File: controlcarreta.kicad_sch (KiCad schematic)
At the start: 38 parts, among them J1 Screw_Terminal_01x02, J1255 Conn_Coaxial, J18 FTDI_AUTOPROG, J2 Screw_Terminal_01x02, J3 Conn_01x04_Male, Q1 SI4447ADY-T1-GE3, Q2 SS8050, Q3 SS8050, SW1 RESET, SW2 BOOT, U1 ESP32-S3-WROOM-1-N8

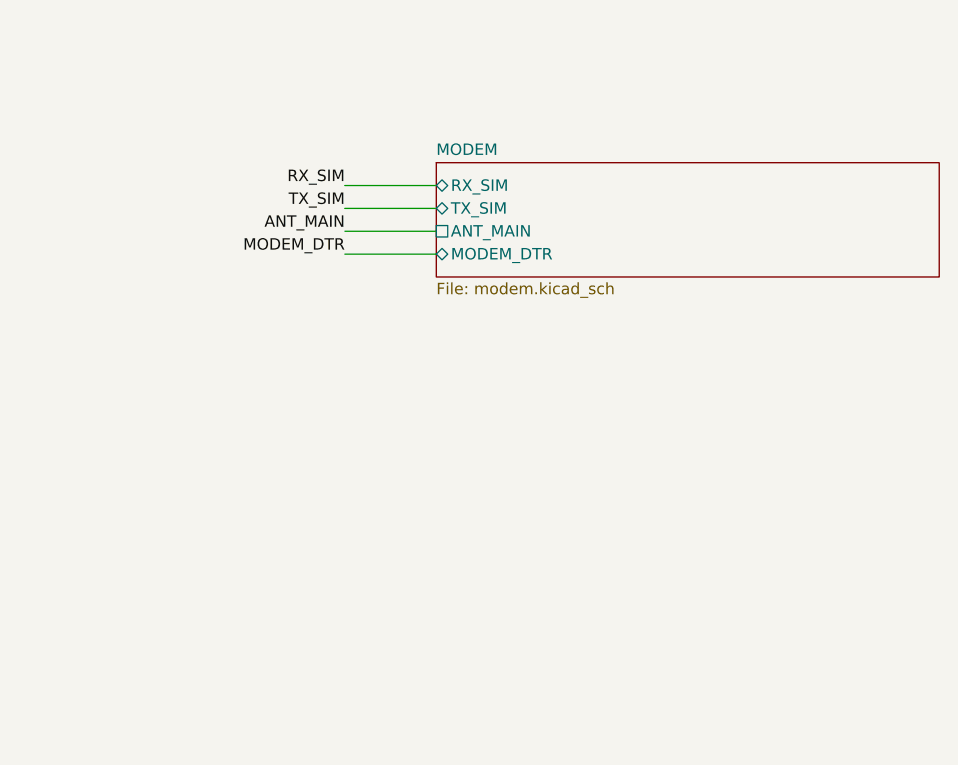
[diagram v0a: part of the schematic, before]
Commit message: modem: 2a via de antena ANT_GNSS (J19 u.FL + J20 SMA) para GPS
El EG25-G / SIM7600 llevan receptor GNSS integrado pero necesitan
antena propia; el esquematico solo tenia ANT_MAIN. Se anade una 2a via
RF identica en topologia a ANT_MAIN:
 - modem.kicad_sch: J19 (u.FL Hirose) -> hierarchical_label ANT_GNSS,
   blindaje a GND (#PWR0563). Pigtail u.FL-u.FL a la toma GNSS de la
   tarjeta Mini-PCIe.
 - controlcarreta.kicad_sch: pin de hoja ANT_GNSS + J20 (SMA Amphenol)
   en la net ANT_GNSS, blindaje a GND (#PWR0564). Caja de la hoja MODEM
   ampliada (12.7 -> 17.78 mm) para alojar los 2 pines nuevos.
 - Poblar J19 O J20 (no ambos). Antena GNSS pasiva, vista al cielo,
   >=3 cm de ANT_MAIN.

ERC sin cambios (370 warnings, 0 errores).

Co-Authored-By: Claude Sonnet 5 <noreply@anthropic.com>
Claude-Session: https://claude.ai/code/session_01T7LXaJdHR17hwkEUJr3uCL
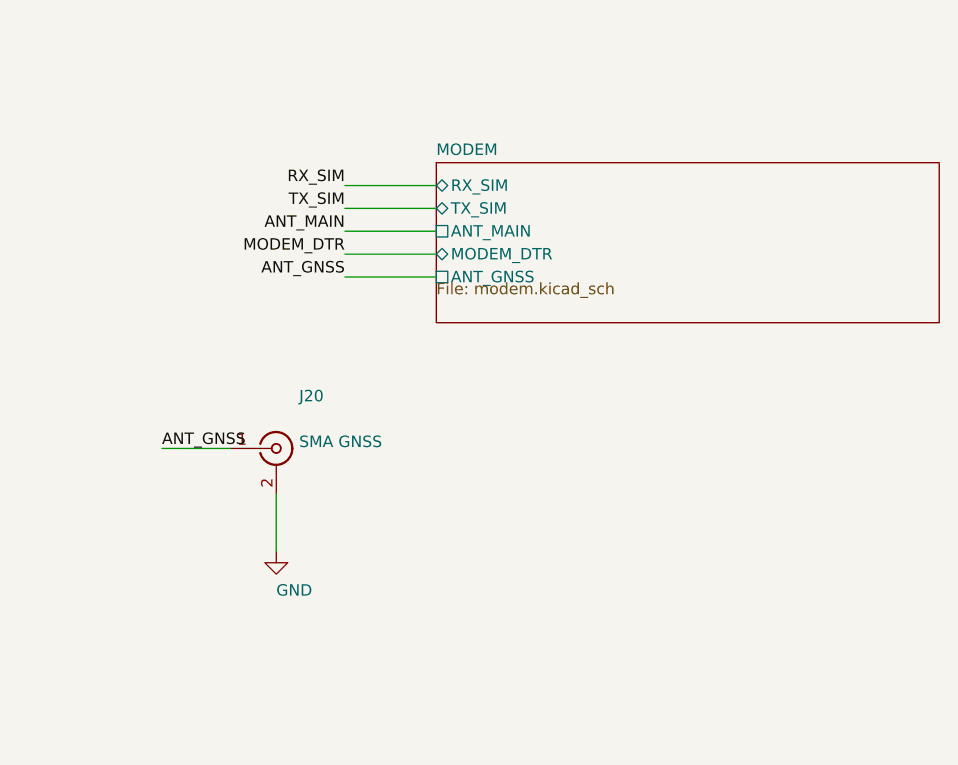
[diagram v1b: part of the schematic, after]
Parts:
- added J20: SMA GNSS, Connector_Coaxial:SMA_Amphenol_132134-16_Vertical, symbol Connector:Conn_Coaxial
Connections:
- net GND: now also J20.2 (Ext)
- new net ANT_GNSS: J20.1 (In)
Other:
- sheet MODEM ports: added ANT_GNSS; removed none
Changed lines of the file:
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@@
 	(wire
 		(pts
+			(xy 330.2 109.22) (xy 320.04 109.22)
+		)
+		(stroke
+			(width 0)
+			(type default)
+		)
+	)
+	(label "ANT_GNSS"
+		(at 320.04 109.22 0)
+		(effects
+			(font
+				(size 1.27 1.27)
+			)
+			(justify right bottom)
+		)
+	)
+	(wire
+		(pts
+			(xy 307.34 128.27) (xy 299.72 128.27)
+		)
+		(stroke
+			(width 0)
+			(type default)
+		)
+	)
+	(label "ANT_GNSS"
+		(at 299.72 128.27 0)
+		(effects
+			(font
+				(size 1.27 1.27)
+			)
+			(justify left bottom)
+		)
+	)
+	(wire
+		(pts
+			(xy 312.42 133.35) (xy 312.42 139.7)
+		)
+		(stroke
+			(width 0)
+			(type default)
+		)
+	)
+	(symbol
+		(lib_id "Connector:Conn_Coaxial")
+		(at 312.42 128.27 0)
+		(unit 1)
+		(exclude_from_sim no)
+		(in_bom yes)
+		(on_board yes)
+		(dnp no)
+		(property "Reference" "J20"
+			(at 314.96 123.19 0)
+			(effects
+				(font
+					(size 1.27 1.27)
+				)
+				(justify left bottom)
+			)
+		)
+		(property "Value" "SMA GNSS"
+			(at 314.96 128.27 0)
+			(effects
+				(font
+					(size 1.27 1.27)
+				)
+				(justify left bottom)
+			)
+		)
+		(property "Footprint" "Connector_Coaxial:SMA_Amphenol_132134-16_Vertical"
+			(at 312.42 128.27 0)
+			(effects
+				(font
+					(size 1.27 1.27)
+				)
+				(justify left bottom)
+				(hide yes)
+			)
+		)
+		(property "Datasheet" "https://www.digikey.com/es/products/detail/amphenol-rf/901-144-8RFX/272189"
+			(at 312.42 128.27 0)
+			(effects
+				(font
+					(size 1.27 1.27)
+				)
+				(justify left bottom)
+				(hide yes)
+			)
+		)
+		(property "Description" "Conector antena GNSS externa (alternativa a J19 u.FL). Antena GNSS pasiva, con vista al cielo, separada >=3 cm de ANT_MAIN."
+			(at 312.42 128.27 0)
+			(effects
+				(font
+					(size 1.27 1.27)
+				)
+				(justify left bottom)
+				(hide yes)
+			)
+		)
+		(property "MPN" "901-144-8RFX"
+			(at 312.42 128.27 0)
+			(effects
+				(font
+					(size 1.27 1.27)
+				)
+				(justify left bottom)
+				(hide yes)
+			)
+		)
+		(property "MANUFACTURER" "Amphenol RF"
+			(at 312.42 128.27 0)
+			(effects
+				(font
+					(size 1.27 1.27)
+				)
+				(justify left bottom)
+				(hide yes)
+			)
+		)
+		(property "BOM Comments" "Poblar J19 (u.FL) O J20 (SMA), no ambos. Solo trazado RF 50ohm entre ambos."
+			(at 312.42 128.27 0)
+			(effects
+				(font
+					(size 1.27 1.27)
+				)
+				(justify left bottom)
+				(hide yes)
+			)
+		)
+		(pin "1"
+		)
+		(pin "2"
+		)
+		(instances
+			(project "controlcarreta"
+				(path "/9232987b-e923-413e-abd9-77ced6cc4c47"
+					(reference "J20")
+					(unit 1)
+				)
+			)
+		)
+	)
+	(symbol
+		(lib_id "power:GND")
+		(at 312.42 139.7 0)
+		(unit 1)
+		(exclude_from_sim no)
+		(in_bom yes)
+		(on_board yes)
+		(dnp no)
+		(property "Reference" "#PWR0564"
+			(at 312.42 146.05 0)
+			(effects
+				(font
+					(size 1.27 1.27)
+				)
+				(justify left bottom)
+				(hide yes)
+			)
+		)
+		(property "Value" "GND"
+			(at 312.42 144.78 0)
+			(effects
+				(font
+					(size 1.27 1.27)
+				)
+				(justify left bottom)
+			)
+		)
+		(property "Footprint" ""
+			(at 312.42 139.7 0)
+			(effects
+				(font
+					(size 1.27 1.27)
+				)
+				(justify left bottom)
+				(hide yes)
+			)
+		)
+		(property "Datasheet" "~"
+			(at 312.42 139.7 0)
+			(effects
+				(font
+					(size 1.27 1.27)
+				)
+				(justify left bottom)
+				(hide yes)
+			)
+		)
+		(property "Description" ""
+			(at 312.42 139.7 0)
+			(effects
+				(font
+					(size 1.27 1.27)
+				)
+				(justify left bottom)
+				(hide yes)
+			)
+		)
+		(pin "1"
+		)
+		(instances
+			(project "controlcarreta"
+				(path "/9232987b-e923-413e-abd9-77ced6cc4c47"
+					(reference "#PWR0564")
+					(unit 1)
+				)
+			)
+		)
+	)
+	(wire
+		(pts
 			(xy 201.295 182.245) (xy 201.295 183.515)
 		)
@@
 	(sheet
 		(at 330.2 96.52)
-		(size 55.88 12.7)
+		(size 55.88 17.78)
 		(exclude_from_sim no)
 		(in_bom yes)
@@
 			(effects
 				(font
+					(size 1.27 1.27)
+				)
+				(justify right)
+			)
+		)
+		(pin "ANT_GNSS" passive
+			(at 330.2 109.22 180)
+			(effects
+				(font
